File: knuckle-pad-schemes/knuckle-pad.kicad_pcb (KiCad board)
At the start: 2 copper layers, 127.6 x 115.3 mm, 67 parts, among them SW1 SW_Push, SW10 SW_Push, SW11 SW_Push, SW12 SW_Push, SW13 SW_Push, SW14 SW_Push, SW15 SW_Push, SW16 SW_Push, SW17 SW_Push, SW18 SW_Push, SW19 SW_Push, SW2 SW_Push, SW20 SW_Push, SW21 SW_Push, SW22 SW_Push, SW23 SW_Push, SW24 SW_Push, SW25 SW_Push, SW26 SW_Push, SW27 SW_Push, SW28 SW_Push, SW29 SW_Push, SW3 SW_Push, SW4 SW_Push, SW5 SW_Push, SW6 SW_Push, SW7 SW_Push, SW8 SW_Push, SW9 SW_Push, U1 ProMicro

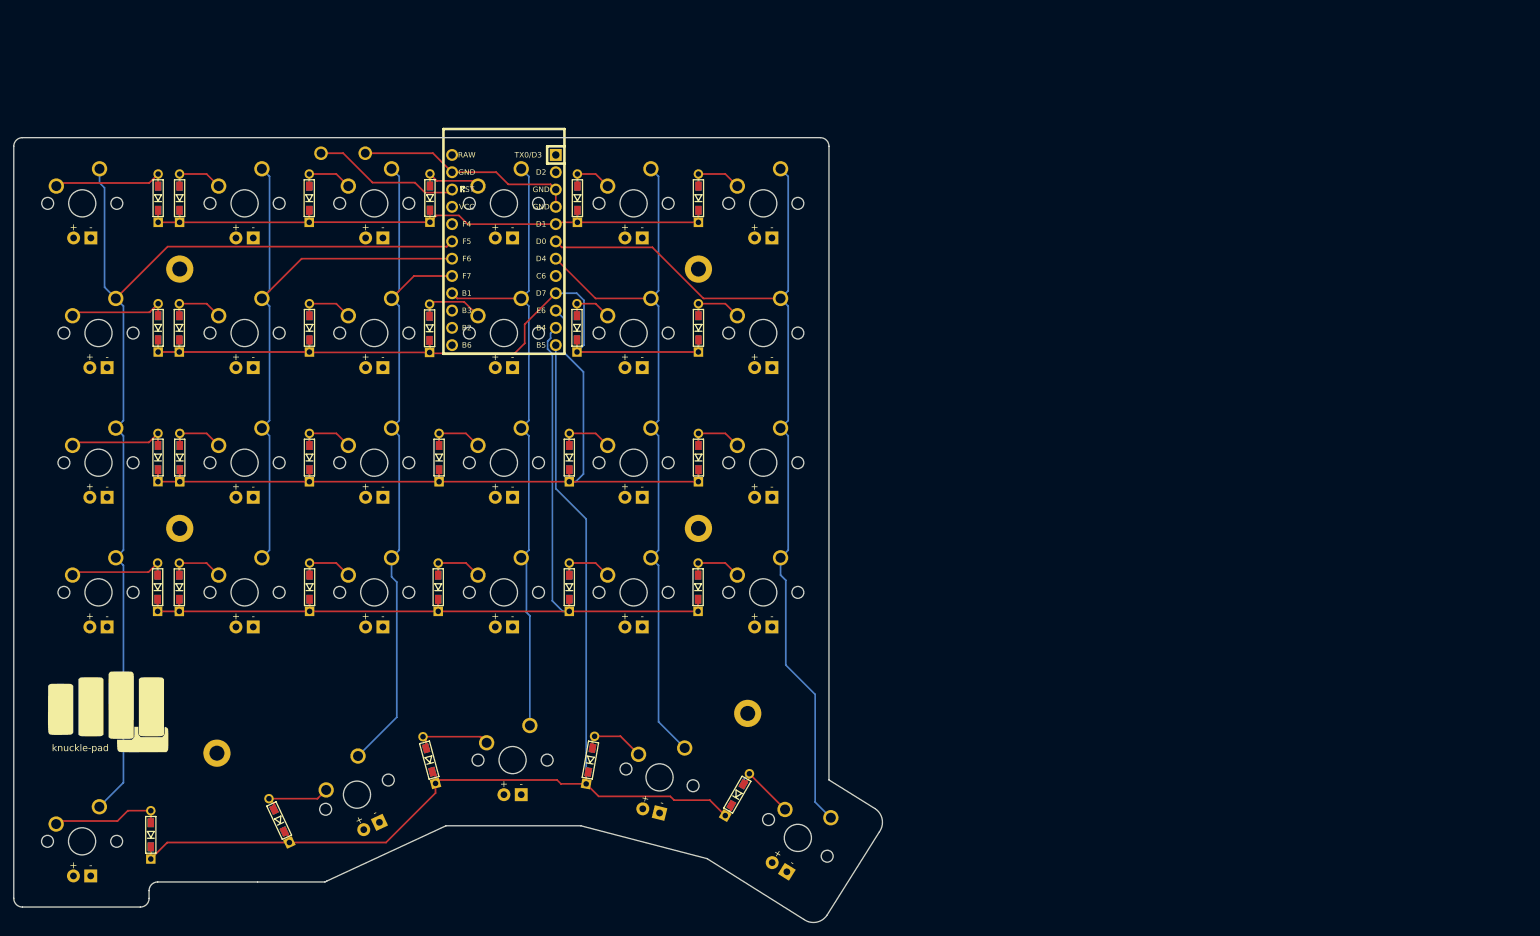
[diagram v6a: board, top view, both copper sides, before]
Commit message: added ground on copper layers
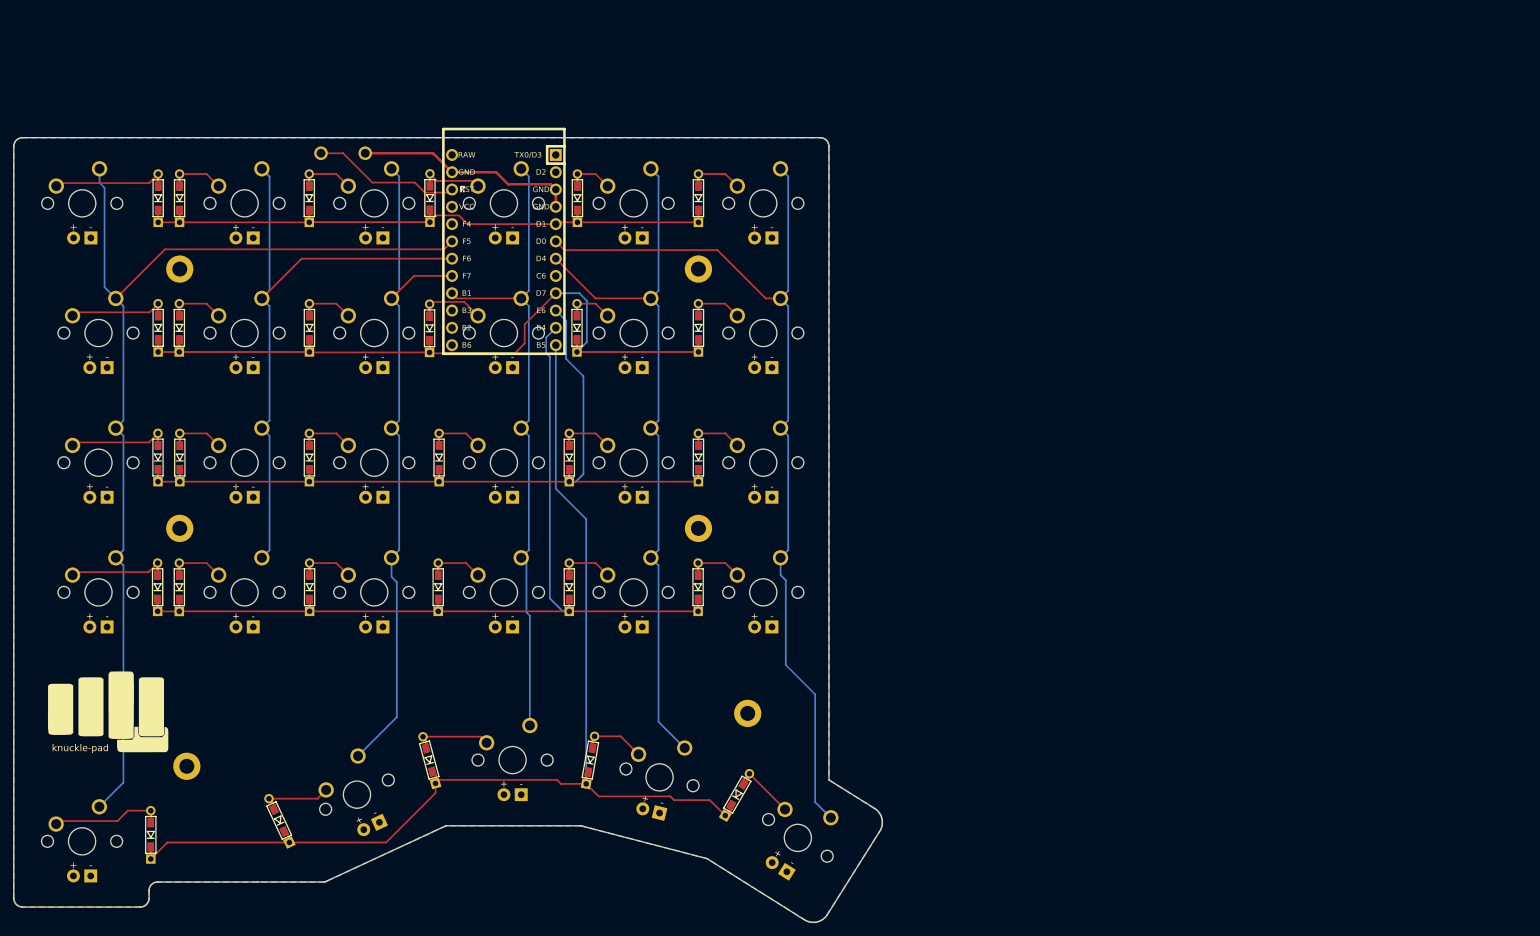
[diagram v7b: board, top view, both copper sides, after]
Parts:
- moved H3 4.82 mm to (106.3, 126.1)
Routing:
- net row1: track 115.5 -> 116.1 mm
- added copper zone on B.Cu, net GND
- added copper zone on F.Cu, net GND

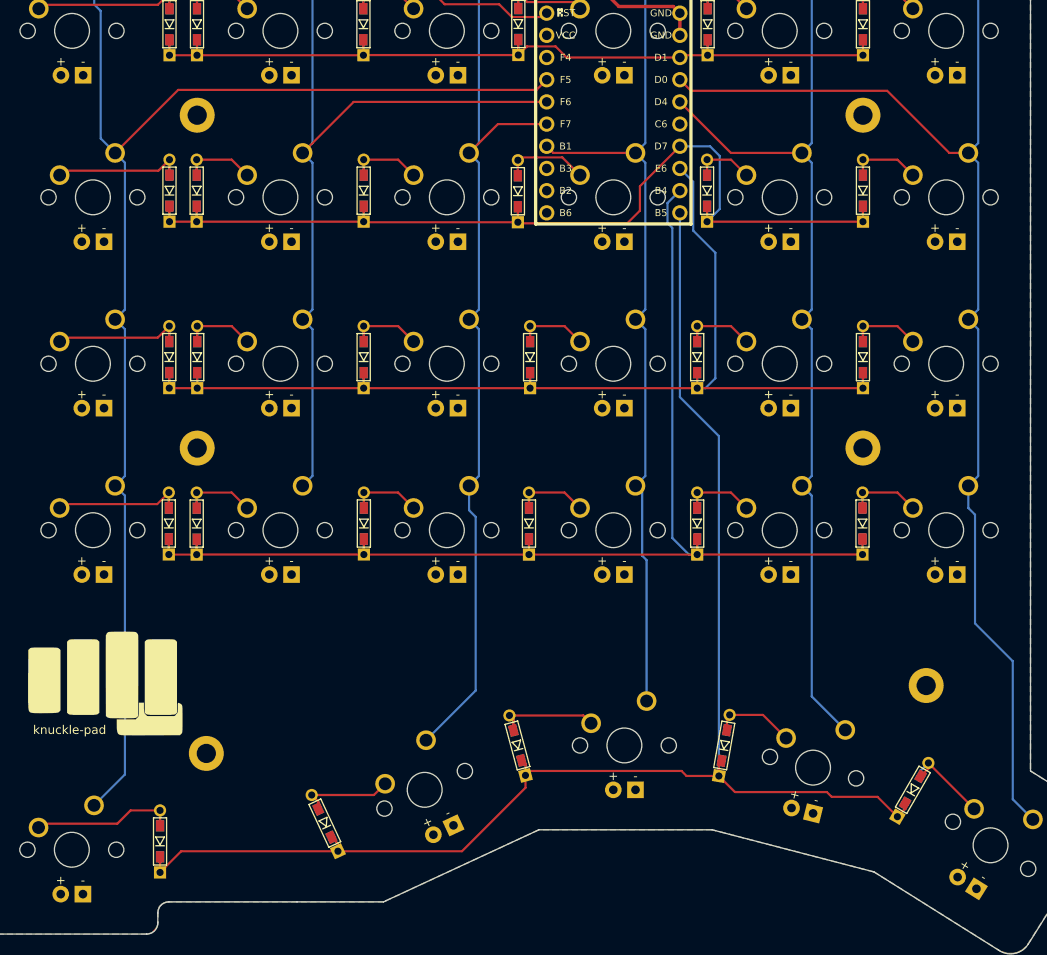
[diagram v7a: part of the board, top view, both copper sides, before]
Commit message: changed switch footprint to mx-NoLed ones
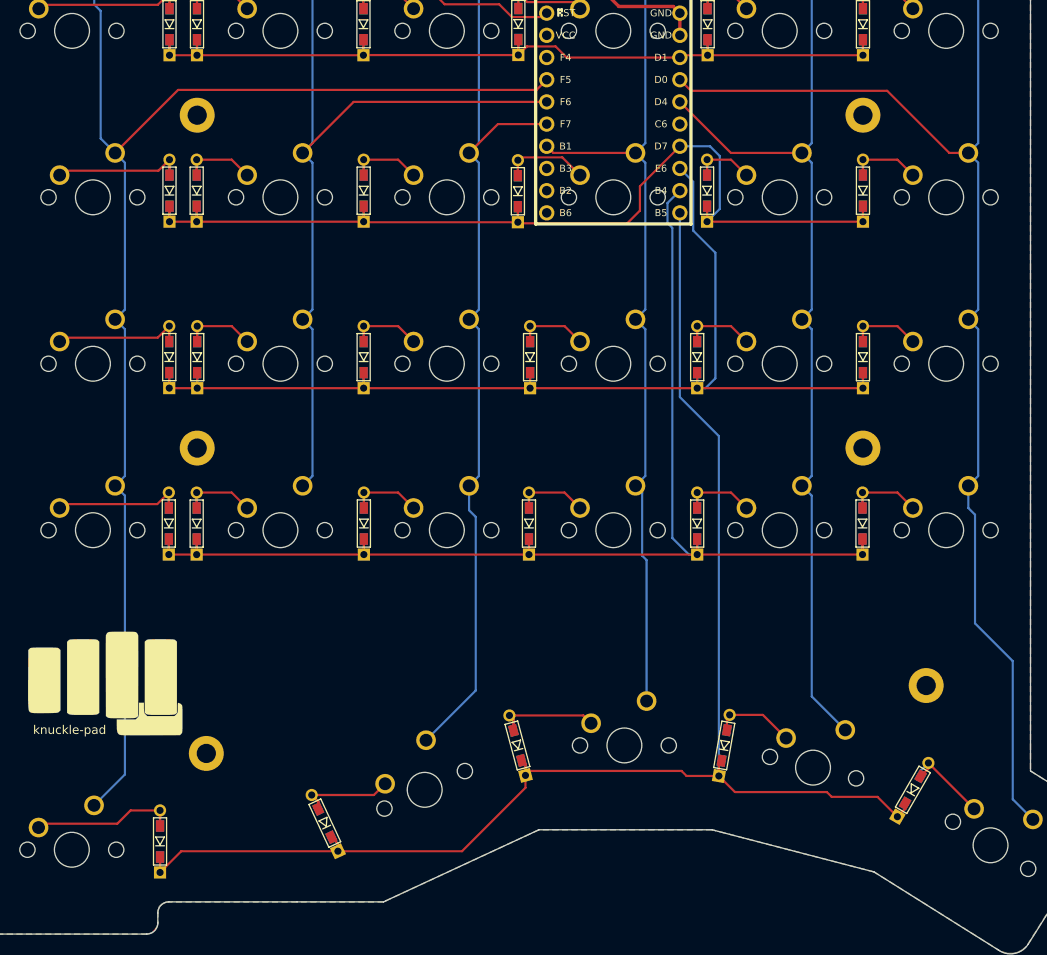
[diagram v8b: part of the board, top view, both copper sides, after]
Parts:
- SW1, SW10, SW11, SW12, SW13, SW14, SW15, SW16, SW17, SW18, SW19, SW20, SW21, SW22, SW23, SW24, SW25, SW26, SW27, SW28, SW29, SW5, SW6, SW7, SW8, SW9: footprint Hybrid-Switches:MX-1u -> MX_Only:MXOnly-1U-NoLED
- SW2, SW3, SW4: footprint Hybrid-Switches:MX-1.25u -> MX_Only:MXOnly-1.25U-NoLED
